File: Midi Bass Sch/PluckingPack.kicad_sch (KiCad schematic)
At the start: 64 parts, among them Q1 BDW93C, Q2 BDW93C, Q3 BDW93C, Q4 BDW93C, Q5 BDW93C, Q6 BDW93C, Q7 BDW93C, Q8 BDW93C, Q89 BDW93C, Q90 BDW93C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

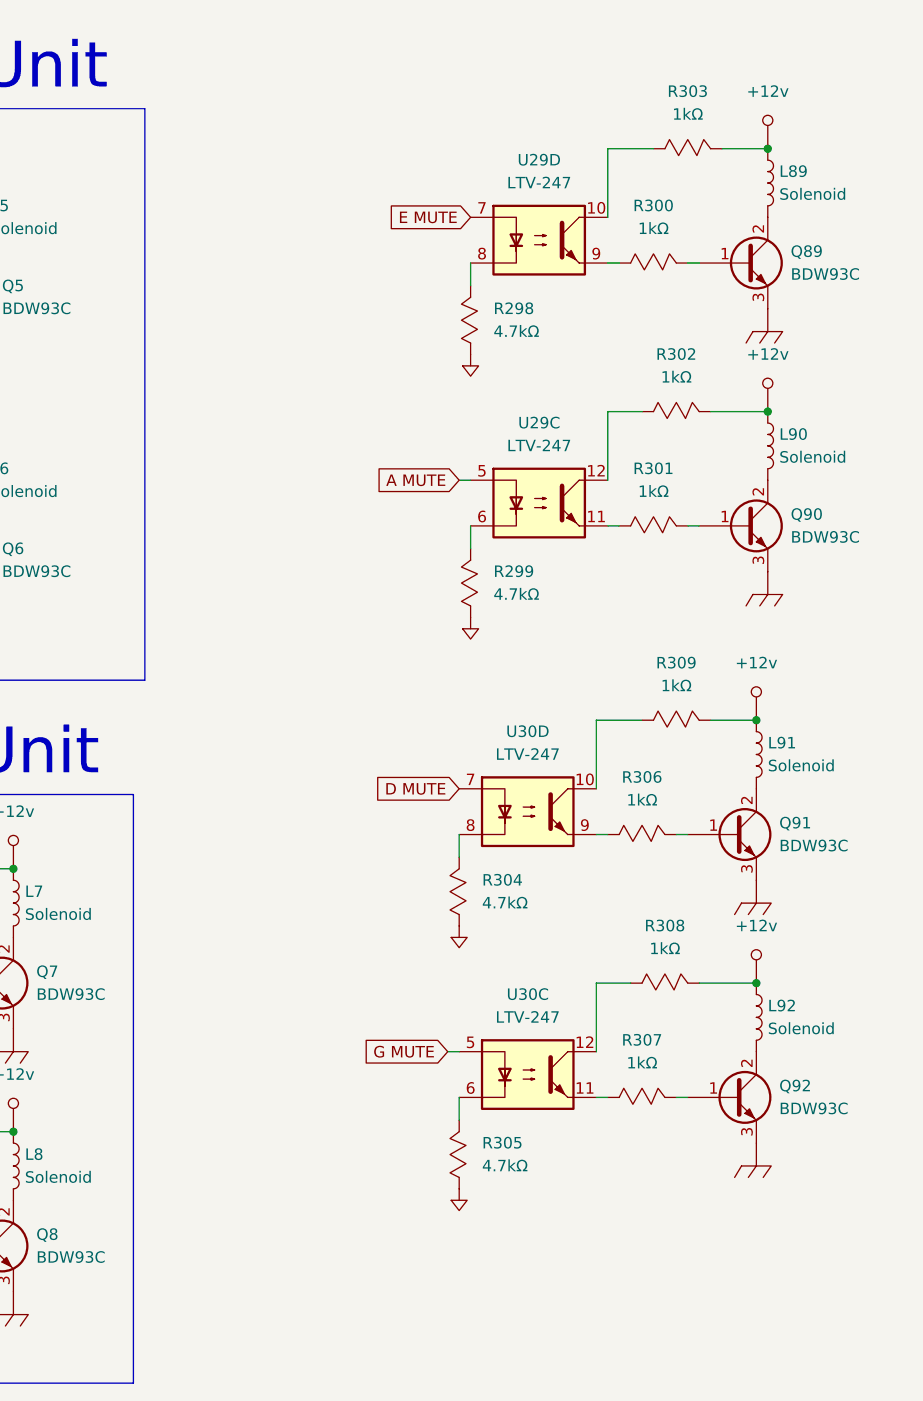
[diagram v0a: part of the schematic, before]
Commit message: finished prelim code for mute implementation
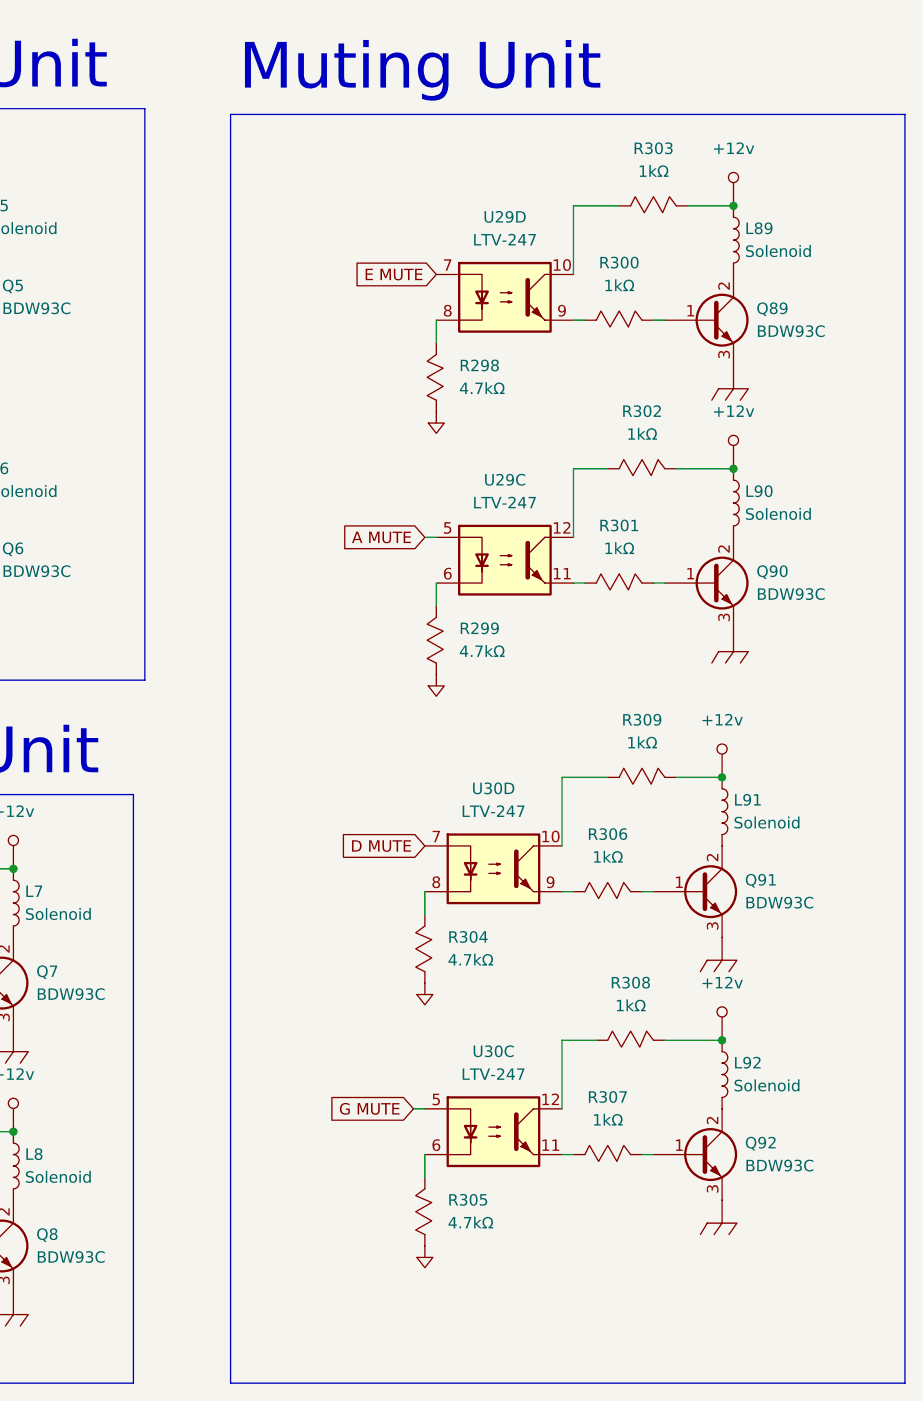
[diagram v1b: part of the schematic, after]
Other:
- note added: "Muting Unit"
- moved on the sheet: L89, L90, L91, L92, Q89, Q90, Q91, Q92, R298, R299, R300, R301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

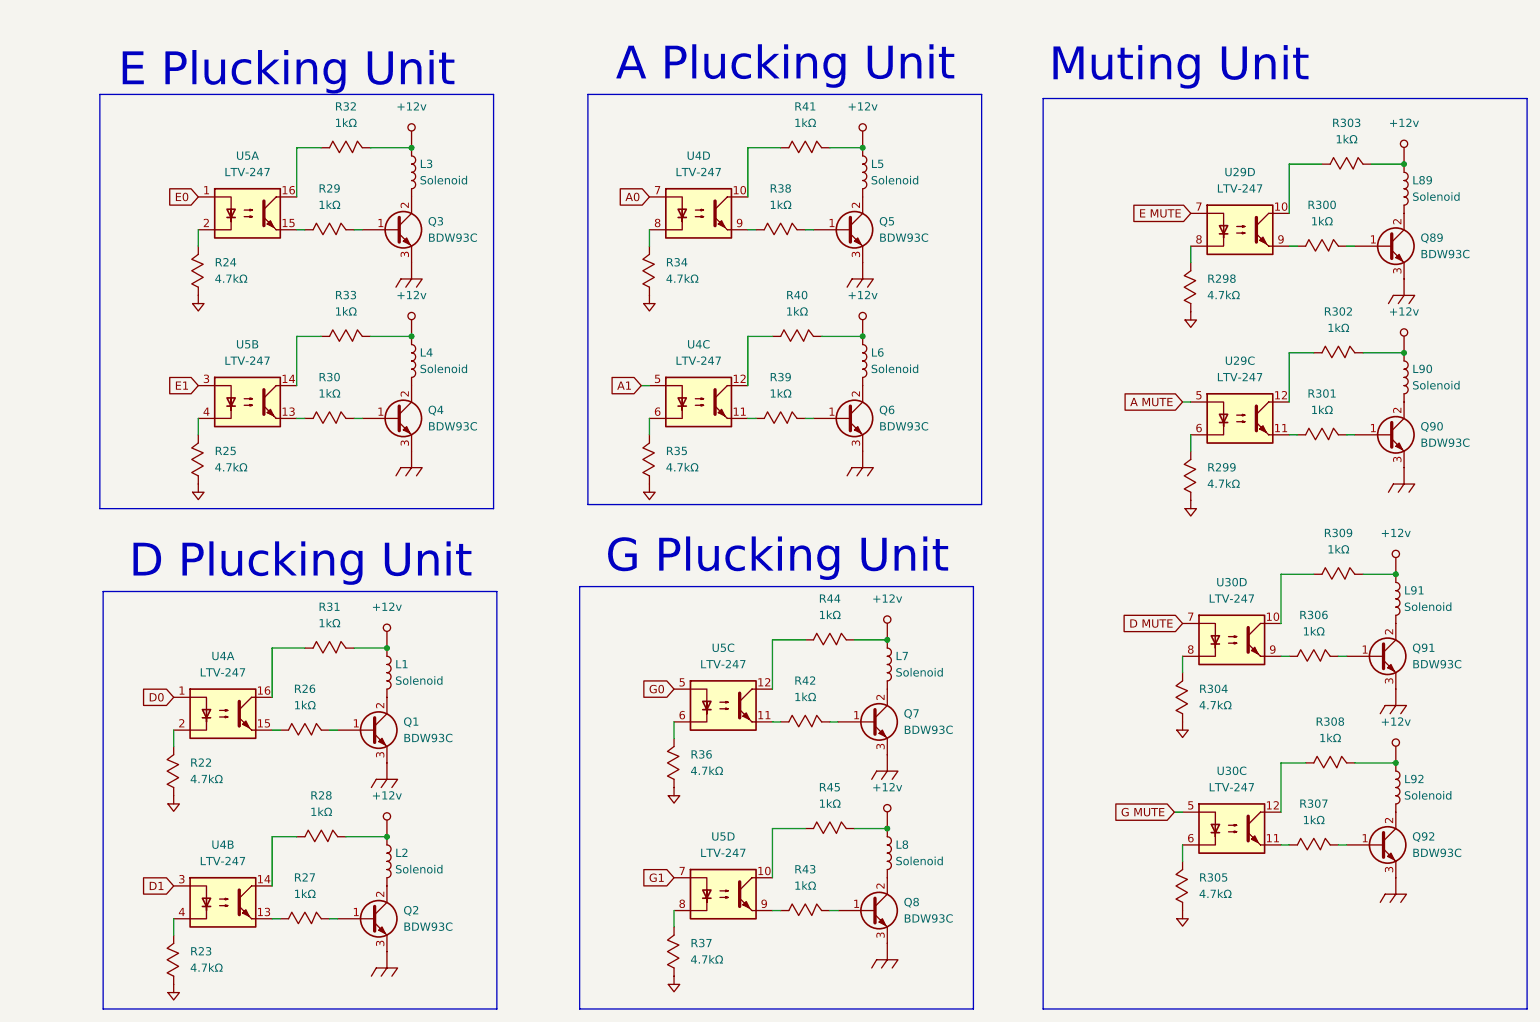
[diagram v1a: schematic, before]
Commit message: updated schematic to reflect code
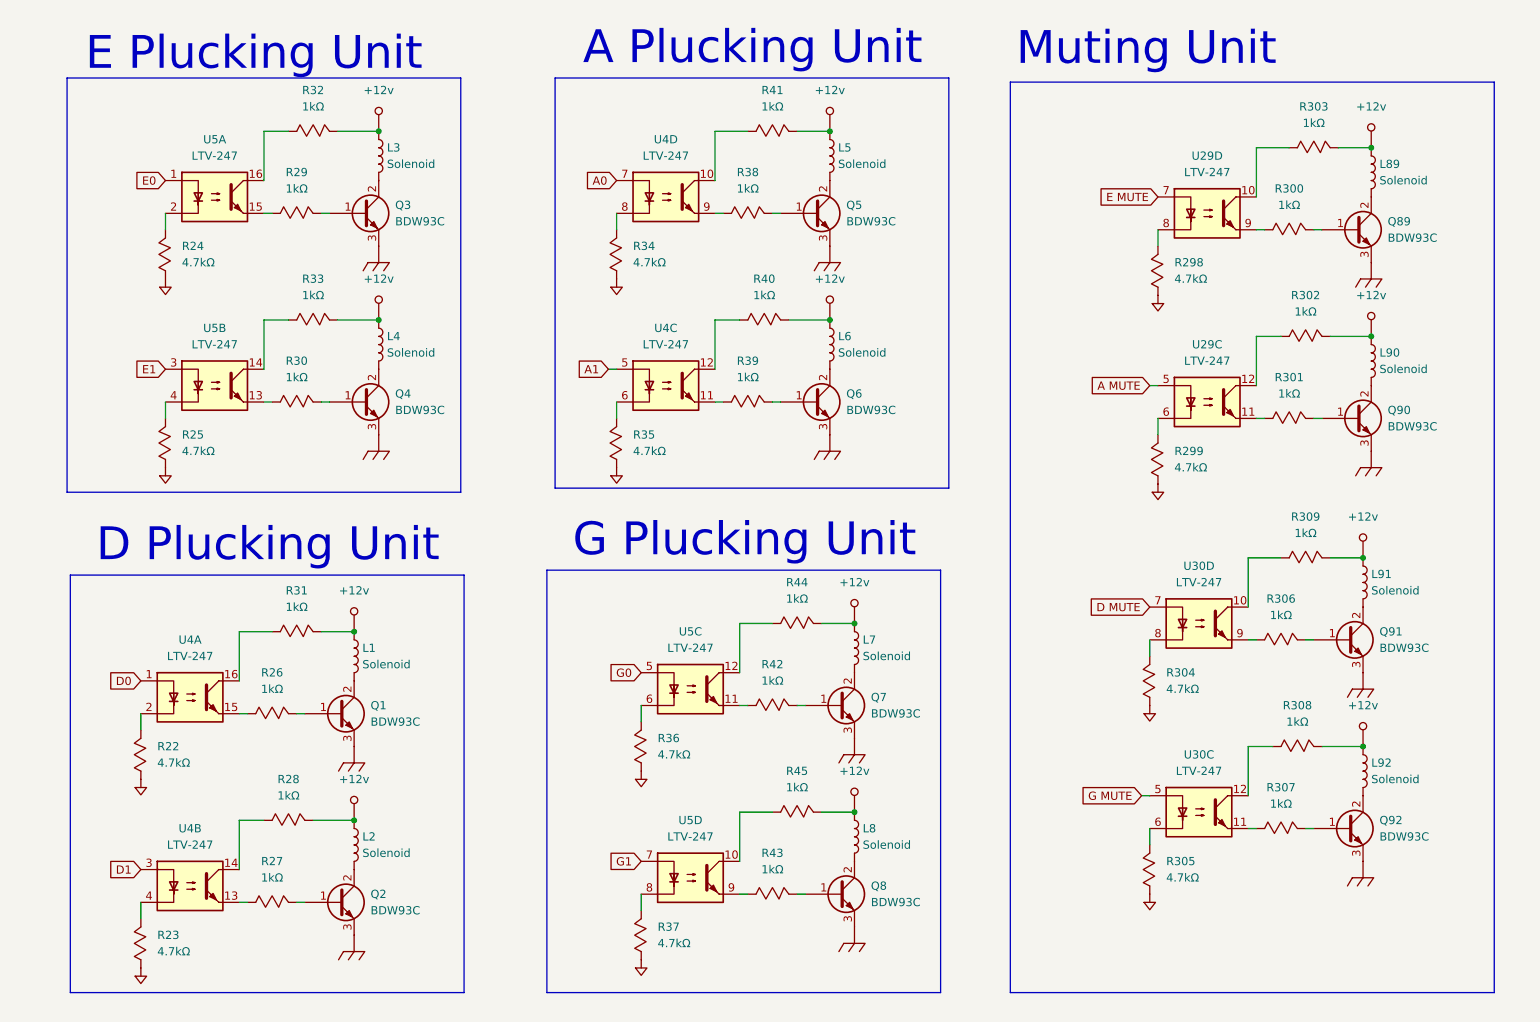
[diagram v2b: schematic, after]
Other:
- moved on the sheet: L1, L2, L3, L4, L5, L6, L7, L8, L89, L90, L91, L92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
